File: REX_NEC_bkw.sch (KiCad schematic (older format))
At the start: 9 parts, among them J1 DIP28 legs 27C256, J2 JTAG, J3 PRG, U1 XCR3064-VQ44, U2 29F800, U3 LP2980

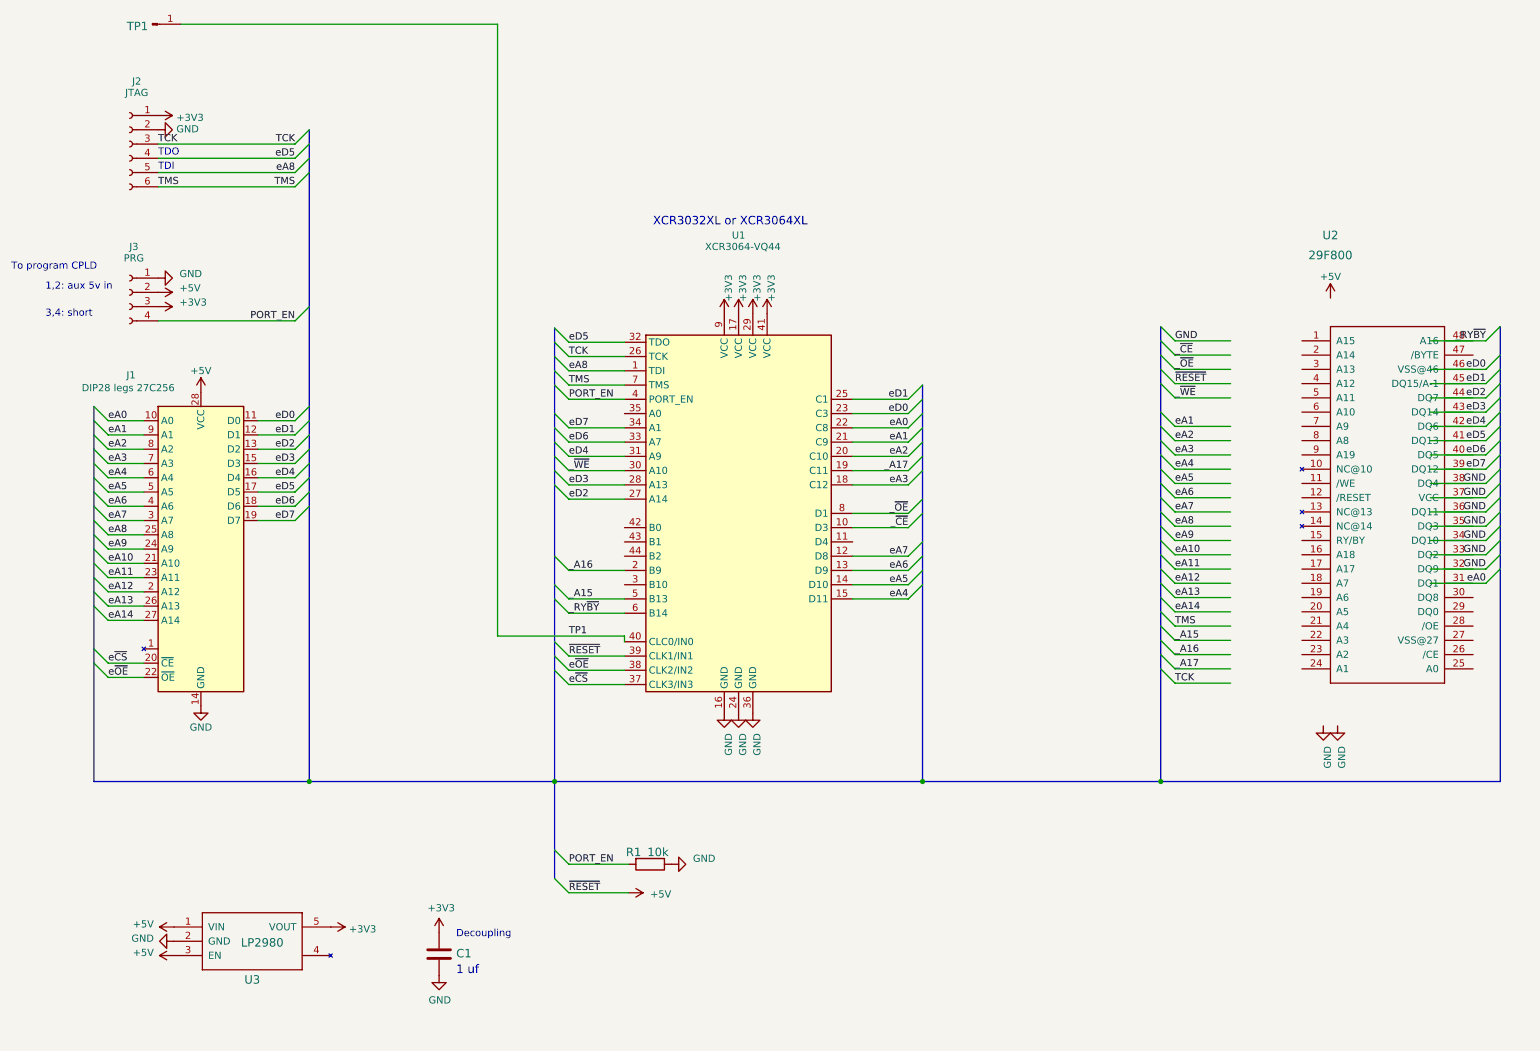
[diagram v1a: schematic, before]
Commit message: flip ram and reroute nec board, several other minor touches both boards
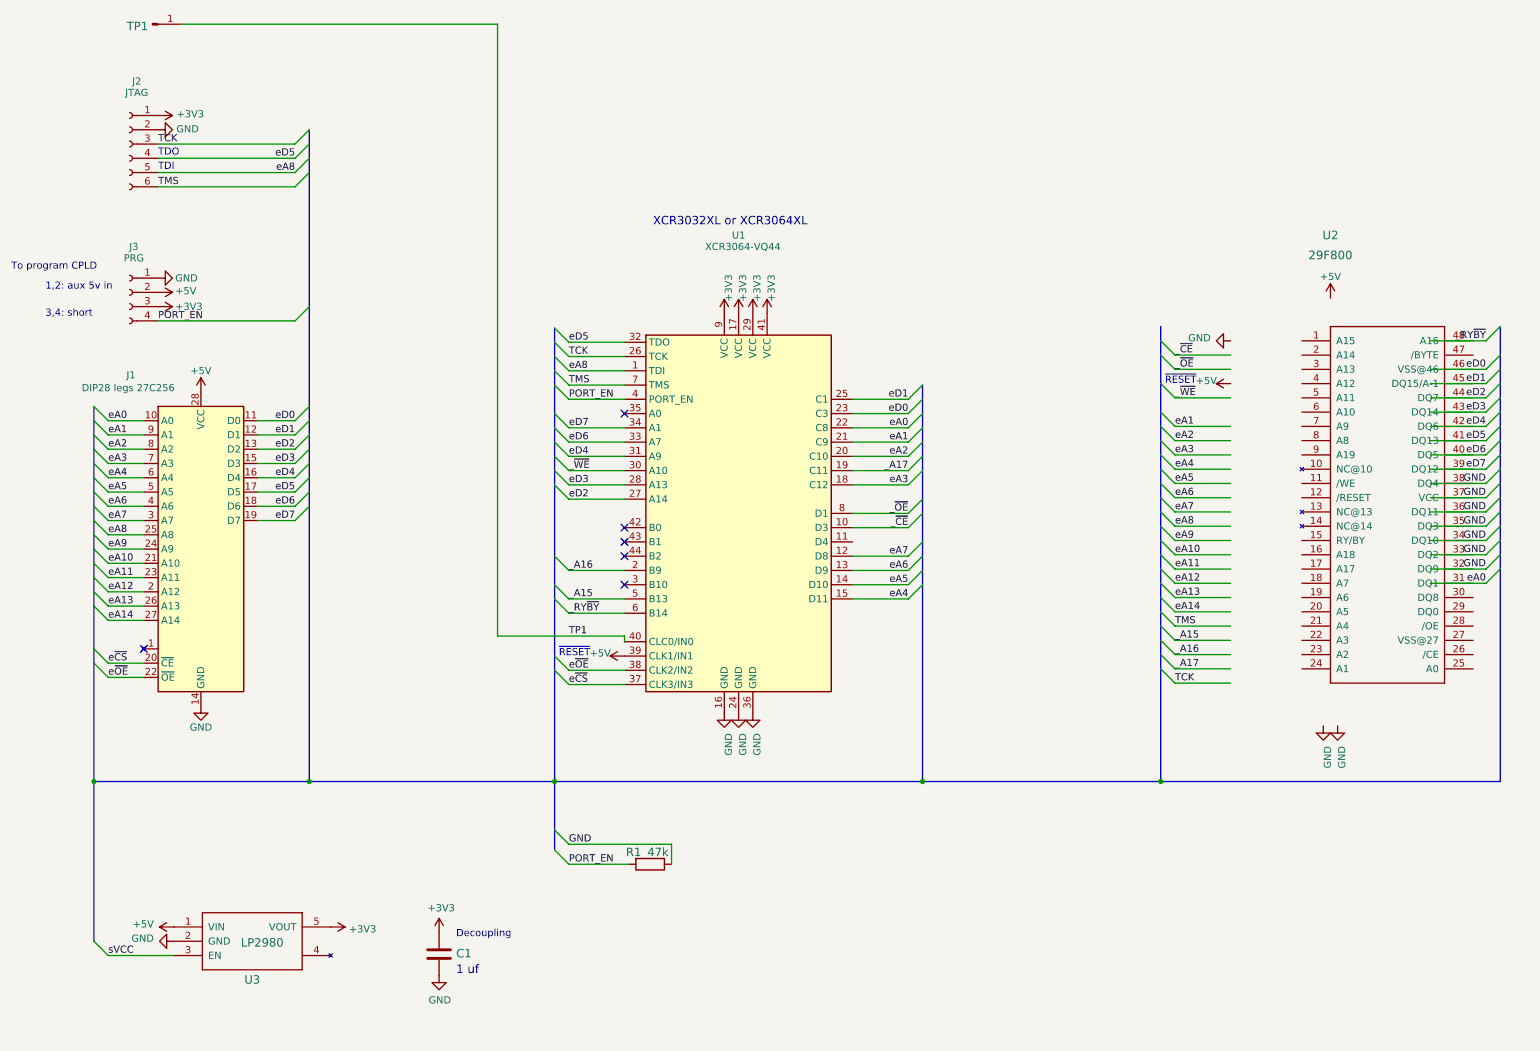
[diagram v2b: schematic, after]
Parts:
- R1: value 10k -> 47k
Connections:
- net labels added: sVCC
- net labels removed: ~RESET
- wire segments 107 -> 106
- no-connect marks 0 -> 6
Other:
- note added: "~RESET"
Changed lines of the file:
@@
 encoding utf-8
 Sheet 1 1
-Title "REX NEC bkw"
-Date "2020-03-23"
-Rev "2"
-Comp ""
-Comment1 "Original: Steven Adolph"
-Comment2 "Modified: Brian White"
+Title "REX NEC, BKW re-spin"
+Date "2020-11-30"
+Rev "4"
+Comp "Brian K. White - b.kenyon.w@gmail.com"
+Comment1 "Original design: Steven Adolph"
+Comment2 ""
 Comment3 ""
 Comment4 ""
@@
 P 7150 7640
 F 0 "R1" V 7100 7470 59  0000 L BNN
-F 1 "10k" V 7100 7620 59  0000 L BNN
+F 1 "47k" V 7100 7620 59  0000 L BNN
 F 2 "000_LOCAL:R_0805" H 7150 7640 50  0001 C CNN
 F 3 "" H 7150 7640 50  0001 C CNN
@@
 Text Notes 7170 3170 0    59   ~ 0
 XCR3032XL or XCR3064XL
-Text Label 4660 3830 2    50   ~ 0
-PORT_EN
 Text Notes 5790 8420 0    60   ~ 0
 1 uf
@@
 P 3700 2390
 F 0 "#PWR0107" H 3700 2240 50  0001 C CNN
-F 1 "+3V3" V 3715 2518 50  0000 L CNN
+F 1 "+3V3" V 3690 2520 50  0000 L CNN
 F 2 "" H 3700 2390 50  0001 C CNN
 F 3 "" H 3700 2390 50  0001 C CNN
@@
 	-1   0    0    -1
 $EndComp
-Text Label 3700 2890 0    50   ~ 0
-TMS
 Wire Wire Line
 	3700 2890 4660 2890
@@
 Wire Wire Line
 	3700 2590 4660 2590
-Text Label 3700 2590 0    50   ~ 0
-TCK
 Entry Wire Line
 	4660 5230 4760 5130
@@
 	0    -1   -1   0
 $EndComp
-$Comp
-L power:+5V #PWR0103
-U 1 1 5EA5EE38
-P 3810 8280
-F 0 "#PWR0103" H 3810 8130 50  0001 C CNN
-F 1 "+5V" V 3830 8420 50  0000 L CNN
-F 2 "" H 3810 8280 50  0001 C CNN
-F 3 "" H 3810 8280 50  0001 C CNN
-	1    3810 8280
-	0    -1   -1   0
-$EndComp
 Wire Wire Line
 	6970 3980 6580 3980
@@
 	11220 5670 10830 5670
 Wire Wire Line
-	11220 3970 10830 3970
-Wire Wire Line
 	11220 4070 10830 4070
 Wire Wire Line
 	11220 4170 10830 4170
 Wire Wire Line
-	11220 4270 10830 4270
-Wire Wire Line
 	11220 4370 10830 4370
 Wire Wire Line
@@
 	10730 6270 10830 6370
 Entry Wire Line
-	10730 3870 10830 3970
-Entry Wire Line
 	10730 3970 10830 4070
 Entry Wire Line
 	10730 4070 10830 4170
-Entry Wire Line
-	10730 4170 10830 4270
 Entry Wire Line
 	10730 4270 10830 4370
@@
 Wire Wire Line
 	6580 7640 7000 7640
-$Comp
-L power:GND #PWR0109
-U 1 1 5EC9316F
-P 7300 7640
-F 0 "#PWR0109" H 7300 7390 50  0001 C CNN
-F 1 "GND" V 7340 7490 50  0000 R CNN
-F 2 "" H 7300 7640 50  0001 C CNN
-F 3 "" H 7300 7640 50  0001 C CNN
-	1    7300 7640
-	0    -1   -1   0
-$EndComp
 $Comp
 L power:+3V3 #PWR0110
@@
 Text Label 13010 5570 2    50   ~ 0
 GND
-Text Label 10830 3970 0    50   ~ 0
-GND
 Text Label 6580 4980 0    50   ~ 0
 eD3
@@
 P 3700 3530
 F 0 "#PWR0122" H 3700 3280 50  0001 C CNN
-F 1 "GND" V 3730 3380 50  0000 R CNN
+F 1 "GND" V 3700 3410 50  0000 R CNN
 F 2 "" H 3700 3530 50  0001 C CNN
 F 3 "" H 3700 3530 50  0001 C CNN
@@
 P 3700 3630
 F 0 "#PWR0123" H 3700 3480 50  0001 C CNN
-F 1 "+5V" V 3670 3780 50  0000 L CNN
+F 1 "+5V" V 3690 3750 50  0000 L CNN
 F 2 "" H 3700 3630 50  0001 C CNN
 F 3 "" H 3700 3630 50  0001 C CNN
@@
 P 3700 3730
 F 0 "#PWR0124" H 3700 3580 50  0001 C CNN
-F 1 "+3V3" V 3670 3880 50  0000 L CNN
+F 1 "+3V3" V 3700 3850 50  0000 L CNN
 F 2 "" H 3700 3730 50  0001 C CNN
 F 3 "" H 3700 3730 50  0001 C CNN
@@
 Text Label 6580 4280 0    50   ~ 0
 TMS
-Text Label 4660 2890 2    50   ~ 0
-TMS
 Text Label 10830 5970 0    50   ~ 0
 TMS
 Text Label 6580 4080 0    50   ~ 0
-TCK
-Text Label 4660 2590 2    50   ~ 0
 TCK
 Text Label 10830 6370 0    50   ~ 0
@@
 Text Notes 3700 2780 0    50   ~ 0
 TDI
-Text Label 10830 4270 0    50   ~ 0
-~RESET
-Entry Wire Line
-	6480 6080 6580 6180
-Text Label 6580 6180 0    50   ~ 0
-~RESET
-Wire Wire Line
-	6580 6180 6970 6180
-Entry Wire Line
-	6480 7740 6580 7840
-Wire Wire Line
-	6580 7840 7000 7840
-Text Label 6580 7840 0    50   ~ 0
-~RESET
-$Comp
-L power:+5V #PWR0125
-U 1 1 5E838367
-P 7000 7840
-F 0 "#PWR0125" H 7000 7690 50  0001 C CNN
-F 1 "+5V" V 7010 7990 50  0000 L CNN
-F 2 "" H 7000 7840 50  0001 C CNN
-F 3 "" H 7000 7840 50  0001 C CNN
-	1    7000 7840
-	0    1    1    0
-$EndComp
 Wire Wire Line
 	6970 6080 6970 6040
@@
 Text Label 6580 6040 0    50   ~ 0
 TP1
+NoConn ~ 6970 5680
+NoConn ~ 6970 5480
+NoConn ~ 6970 5380
+NoConn ~ 6970 5280
+NoConn ~ 6970 4480
+NoConn ~ 3600 6130
 Wire Bus Line
-	6480 7060 6480 7740
+	3250 7060 3250 8180
+Connection ~ 3250 7060
+Entry Wire Line
+	3250 8180 3350 8280
+Wire Wire Line
+	3350 8280 3810 8280
+Text Label 3350 8280 0    50   ~ 0
+sVCC
+Entry Wire Line
+	6480 7400 6580 7500
+Wire Wire Line
+	7300 7640 7300 7500
+Wire Wire Line
+	7300 7500 6580 7500
+Text Label 6580 7500 0    50   ~ 0
+GND
+Text Label 3700 2590 0    50   ~ 0
+TCK
+Text Label 3700 2890 0    50   ~ 0
+TMS
+Text Label 3700 3830 0    50   ~ 0
+PORT_EN
+Text Notes 6510 6190 0    50   ~ 0
+~RESET
+$Comp
+L power:+5V #PWR?
+U 1 1 5FD817E1
+P 6970 6180
+F 0 "#PWR?" H 6970 6030 50  0001 C CNN
+F 1 "+5V" V 6990 6350 50  0000 C CNN
+F 2 "" H 6970 6180 50  0001 C CNN
+F 3 "" H 6970 6180 50  0001 C CNN
+	1    6970 6180
+	0    -1   -1   0
+$EndComp
+Text Notes 10760 4280 0    50   ~ 0
+~RESET
+$Comp
+L power:+5V #PWR?
+U 1 1 5FD8D230
+P 11220 4270
+F 0 "#PWR?" H 11220 4120 50  0001 C CNN
+F 1 "+5V" V 11240 4440 50  0000 C CNN
+F 2 "" H 11220 4270 50  0001 C CNN
+F 3 "" H 11220 4270 50  0001 C CNN
+	1    11220 4270
+	0    -1   -1   0
+$EndComp
+$Comp
+L power:GND #PWR?
+U 1 1 5FDCE74B
+P 11220 3970
+F 0 "#PWR?" H 11220 3720 50  0001 C CNN
+F 1 "GND" V 11200 3830 50  0000 R CNN
+F 2 "" H 11220 3970 50  0001 C CNN
+F 3 "" H 11220 3970 50  0001 C CNN
+	1    11220 3970
+	0    1    1    0
+$EndComp
+Wire Bus Line
+	6480 7060 6480 7540
 Wire Bus Line
 	4760 2490 4760 7060

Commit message: Less expensive manufacturing tolerances. Rename to REX Classic.
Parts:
- added NT1, NT2, NT3: Net-Tie_2, 000_LOCAL:Net_Tie_2_0.18mm, symbol 000_LOCAL:Net-Tie_2
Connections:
- net labels added: EN, ~RESET_U1, ~RESET_U2
- net labels removed: sVCC
- wire segments 106 -> 105
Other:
- note removed: "~RESET"
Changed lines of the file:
@@
 Sheet 1 1
 Title "REX NEC, BKW re-spin"
-Date "2020-11-30"
-Rev "4"
+Date "2021-03-07"
+Rev "5"
 Comp "Brian K. White - b.kenyon.w@gmail.com"
 Comment1 "Original design: Steven Adolph"
@@
 NoConn ~ 6970 4480
 NoConn ~ 3600 6130
-Wire Bus Line
-	3250 7060 3250 8180
-Connection ~ 3250 7060
-Entry Wire Line
-	3250 8180 3350 8280
-Wire Wire Line
-	3350 8280 3810 8280
-Text Label 3350 8280 0    50   ~ 0
-sVCC
 Entry Wire Line
 	6480 7400 6580 7500
@@
 Text Label 3700 3830 0    50   ~ 0
 PORT_EN
-Text Notes 6510 6190 0    50   ~ 0
-~RESET
-$Comp
-L power:+5V #PWR?
-U 1 1 5FD817E1
-P 6970 6180
-F 0 "#PWR?" H 6970 6030 50  0001 C CNN
-F 1 "+5V" V 6990 6350 50  0000 C CNN
-F 2 "" H 6970 6180 50  0001 C CNN
-F 3 "" H 6970 6180 50  0001 C CNN
-	1    6970 6180
-	0    -1   -1   0
-$EndComp
-Text Notes 10760 4280 0    50   ~ 0
-~RESET
-$Comp
-L power:+5V #PWR?
-U 1 1 5FD8D230
-P 11220 4270
-F 0 "#PWR?" H 11220 4120 50  0001 C CNN
-F 1 "+5V" V 11240 4440 50  0000 C CNN
-F 2 "" H 11220 4270 50  0001 C CNN
-F 3 "" H 11220 4270 50  0001 C CNN
-	1    11220 4270
-	0    -1   -1   0
-$EndComp
-$Comp
-L power:GND #PWR?
+$Comp
+L power:GND #PWR0125
 U 1 1 5FDCE74B
 P 11220 3970
-F 0 "#PWR?" H 11220 3720 50  0001 C CNN
+F 0 "#PWR0125" H 11220 3720 50  0001 C CNN
 F 1 "GND" V 11200 3830 50  0000 R CNN
 F 2 "" H 11220 3970 50  0001 C CNN
@@
 	0    1    1    0
 $EndComp
+$Comp
+L power:+5V #PWR0126
+U 1 1 6049858A
+P 3610 8280
+F 0 "#PWR0126" H 3610 8130 50  0001 C CNN
+F 1 "+5V" V 3630 8420 50  0000 L CNN
+F 2 "" H 3610 8280 50  0001 C CNN
+F 3 "" H 3610 8280 50  0001 C CNN
+	1    3610 8280
+	0    -1   -1   0
+$EndComp
+$Comp
+L 000_LOCAL:Net-Tie_2 NT1
+U 1 1 6049F9B3
+P 3710 8280
+F 0 "NT1" H 3710 8240 50  0001 C CNN
+F 1 "Net-Tie_2" H 3720 8410 50  0001 C CNN
+F 2 "000_LOCAL:Net_Tie_2_0.18mm" H 3710 8280 50  0001 C CNN
+F 3 "~" H 3710 8280 50  0001 C CNN
+	1    3710 8280
+	1    0    0    -1
+$EndComp
+Text Label 3810 8280 2    50   ~ 0
+EN
+$Comp
+L power:+5V #PWR0109
+U 1 1 604B6F92
+P 11020 4270
+F 0 "#PWR0109" H 11020 4120 50  0001 C CNN
+F 1 "+5V" V 11040 4410 50  0000 L CNN
+F 2 "" H 11020 4270 50  0001 C CNN
+F 3 "" H 11020 4270 50  0001 C CNN
+	1    11020 4270
+	0    -1   -1   0
+$EndComp
+$Comp
+L 000_LOCAL:Net-Tie_2 NT2
+U 1 1 604B6FEA
+P 11120 4270
+F 0 "NT2" H 11120 4230 50  0001 C CNN
+F 1 "Net-Tie_2" H 11130 4400 50  0001 C CNN
+F 2 "000_LOCAL:Net_Tie_2_0.18mm" H 11120 4270 50  0001 C CNN
+F 3 "~" H 11120 4270 50  0001 C CNN
+	1    11120 4270
+	1    0    0    -1
+$EndComp
+Text Label 11220 4270 2    50   ~ 0
+~RESET_U2
+$Comp
+L power:+5V #PWR0103
+U 1 1 604EC72A
+P 6770 6180
+F 0 "#PWR0103" H 6770 6030 50  0001 C CNN
+F 1 "+5V" V 6790 6320 50  0000 L CNN
+F 2 "" H 6770 6180 50  0001 C CNN
+F 3 "" H 6770 6180 50  0001 C CNN
+	1    6770 6180
+	0    -1   -1   0
+$EndComp
+$Comp
+L 000_LOCAL:Net-Tie_2 NT3
+U 1 1 604EC85E
+P 6870 6180
+F 0 "NT3" H 6870 6140 50  0001 C CNN
+F 1 "Net-Tie_2" H 6880 6310 50  0001 C CNN
+F 2 "000_LOCAL:Net_Tie_2_0.18mm" H 6870 6180 50  0001 C CNN
+F 3 "~" H 6870 6180 50  0001 C CNN
+	1    6870 6180
+	1    0    0    -1
+$EndComp
+Text Label 6970 6180 2    50   ~ 0
+~RESET_U1
 Wire Bus Line
 	6480 7060 6480 7540
@@
 	13110 3870 13110 7060
 Wire Bus Line
+	10730 3870 10730 7060
+Wire Bus Line
 	6480 3880 6480 7060
 Wire Bus Line
 	3250 4430 3250 7060
-Wire Bus Line
-	10730 3870 10730 7060
 $EndSCHEMATC

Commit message: clearances, remove pointless busses in schematic
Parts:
- C1: value C-USC0805 -> 1u
- U1: footprint 000_LOCAL:QFP44 -> 000_LOCAL:VQFP44; symbol 000_LOCAL:XCR3064-VQ44 -> 000_LOCAL:XCR3064XL-VQ44_kicad
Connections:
- wire segments 105 -> 0
- no-connect marks 6 -> 7
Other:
- note added: "29F800 bottom boot"
- note removed: "1 uf"
- moved on the sheet: TP1
